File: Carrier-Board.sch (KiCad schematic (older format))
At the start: 39 parts, among them J1 CONN_3-6318491-6, J2 Conn_01x0, J3 Conn_02x26_Odd_Even, J4 SI-51009-F, J5 Conn_02x26_Odd_Even, J6 Conn_01x03_Male, J7 Conn_01x03_Male, J8 Conn_01x06_Male, J9 Conn_02x04_Odd_Even, U1 MPM3620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

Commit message: Notes
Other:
- note added: "Pixie Wranglers:\nPrabodh Jhaveri \nChandler Griscom\n"
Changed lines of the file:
@@
 Text Notes 11600 700  0    60   ~ 0
 PC104\n
+Text Notes 9450 10900 0    60   ~ 0
+Pixie Wranglers:\nPrabodh Jhaveri \nChandler Griscom\n
 $EndSCHEMATC

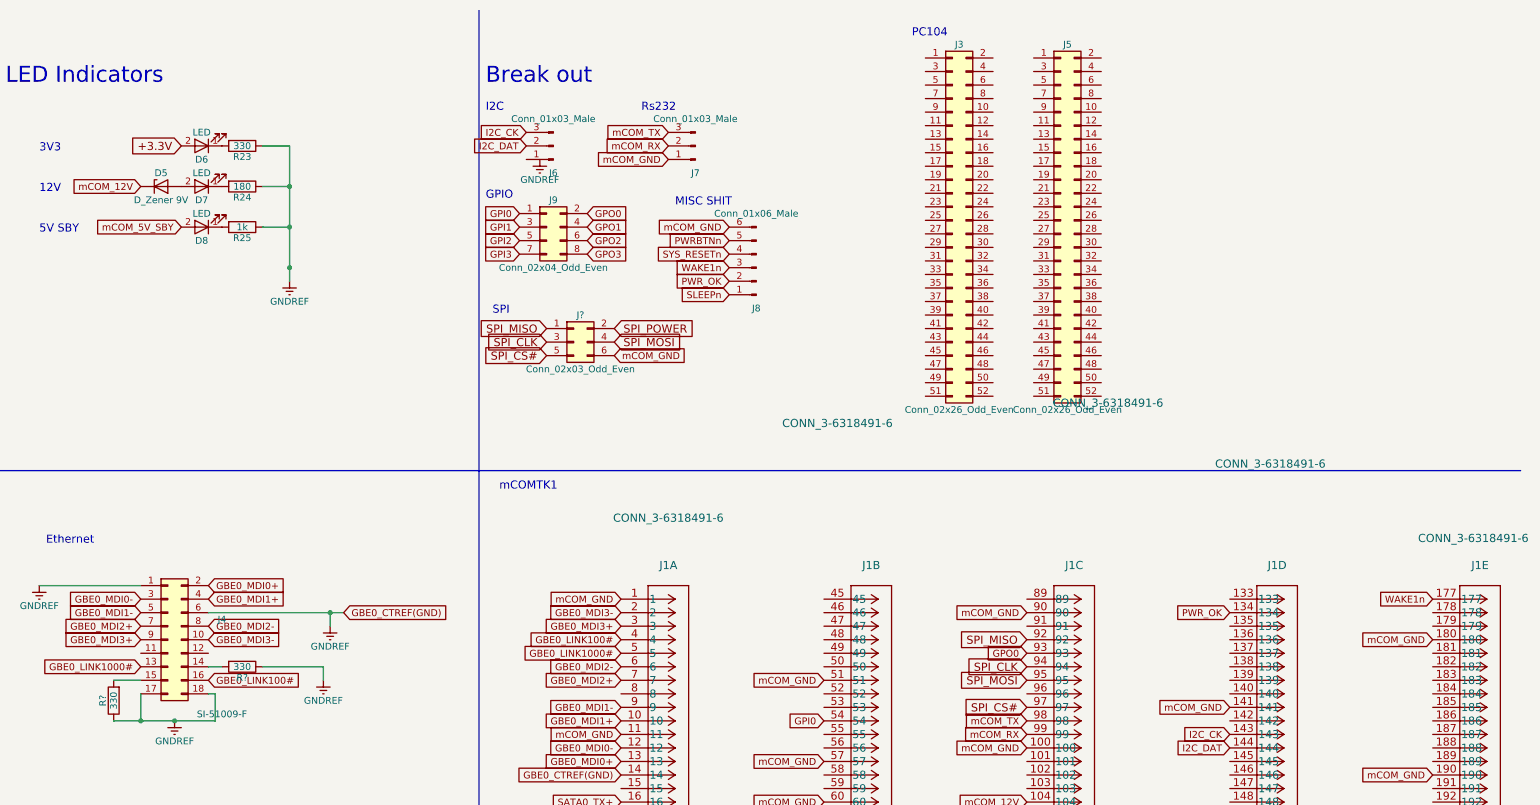
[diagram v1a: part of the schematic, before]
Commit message: added buttons
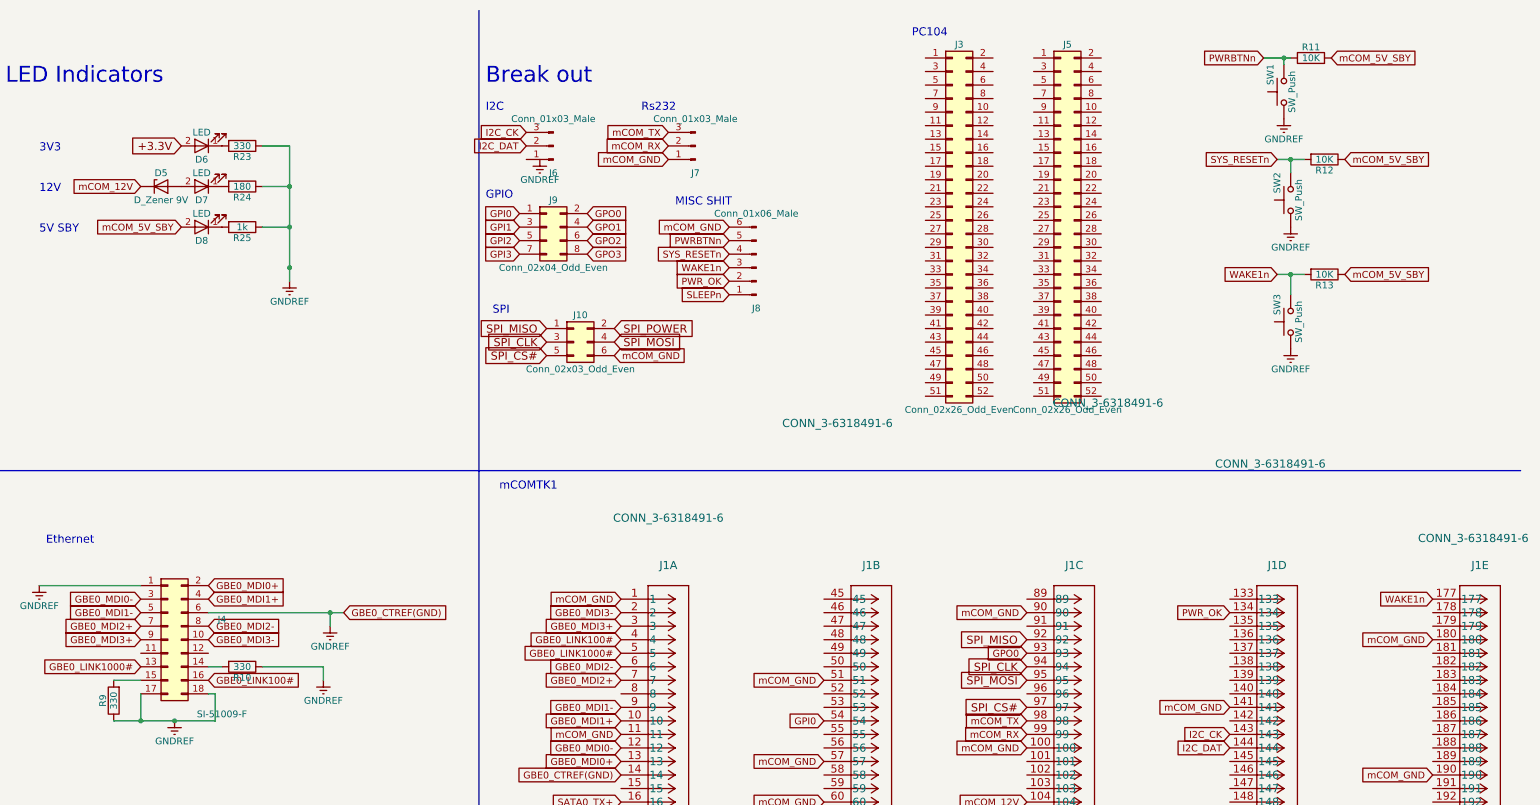
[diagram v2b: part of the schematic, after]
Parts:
- added R11, R12, R13: 10K, symbol R
- added SW1, SW2, SW3: SW_Push, Buttons_Switches_SMD:SW_SPST_PTS645, symbol SW_Push
- J10: renamed from J?; footprint (none) -> Pin_Headers:Pin_Header_Angled_2x03_Pitch2.54mm
- gave numbers to parts that had none: 2
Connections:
- net +5V: now also R11.2, R12.1, R13.1
- net GNDREF: now also SW1.1, SW2.1, SW3.1
- net PWRBTNn: now also R11.1, SW1.2
- net SYS_RESETn: now also R12.2, SW2.2
- net WAKE1n: now also R13.2, SW3.2

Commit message: Change but3ton footprint
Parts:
- SW1, SW2, SW3: footprint Buttons_Switches_SMD:SW_SPST_PTS645 -> Buttons_Switches_SMD:SW_SPST_B3U-1000P
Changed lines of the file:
@@
 LIBS:Carrier-Board
 LIBS:SI-51009-F
+LIBS:MCP6H04-E
+LIBS:BusSimulator
 LIBS:Carrier-Board-cache
 EELAYER 25 0
@@
 F 0 "SW2" H 14450 2000 50  0000 L CNN
 F 1 "SW_Push" H 14400 1840 50  0000 C CNN
-F 2 "Buttons_Switches_SMD:SW_SPST_PTS645" H 14400 2100 50  0001 C CNN
+F 2 "Buttons_Switches_SMD:SW_SPST_B3U-1000P" H 14400 2100 50  0001 C CNN
 F 3 "" H 14400 2100 50  0001 C CNN
 	1    14400 1900
@@
 F 0 "SW3" H 14450 2900 50  0000 L CNN
 F 1 "SW_Push" H 14400 2740 50  0000 C CNN
-F 2 "Buttons_Switches_SMD:SW_SPST_PTS645" H 14400 3000 50  0001 C CNN
+F 2 "Buttons_Switches_SMD:SW_SPST_B3U-1000P" H 14400 3000 50  0001 C CNN
 F 3 "" H 14400 3000 50  0001 C CNN
 	1    14400 2800
@@
 F 0 "SW1" H 14400 1200 50  0000 L CNN
 F 1 "SW_Push" H 14350 1040 50  0000 C CNN
-F 2 "Buttons_Switches_SMD:SW_SPST_PTS645" H 14350 1300 50  0001 C CNN
+F 2 "Buttons_Switches_SMD:SW_SPST_B3U-1000P" H 14350 1300 50  0001 C CNN
 F 3 "" H 14350 1300 50  0001 C CNN
 	1    14350 1100

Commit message: started traces
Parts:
- C1, C2, C3, C4: footprint BusSimulator:C22 -> Capacitors_SMD:C_0805
- R10: footprint (none) -> Resistors_SMD:R_0805
- R11, R12, R13: footprint (none) -> Resistors_SMD:R_0603
- renumbered D7 to D6, D6 to D7
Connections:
- net GNDREF: now also J6.1 (Pin_1)
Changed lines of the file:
@@
 LIBS:Carrier-Board
 LIBS:SI-51009-F
-LIBS:MCP6H04-E
-LIBS:BusSimulator
 LIBS:Carrier-Board-cache
 EELAYER 25 0
@@
 F 0 "C2" V 3075 3625 60  0000 C CNN
 F 1 "22uF" V 3000 3575 60  0000 C CNN
-F 2 "BusSimulator:C22" H 3150 3040 60  0001 C CNN
+F 2 "Capacitors_SMD:C_0805" H 3150 3040 60  0001 C CNN
 F 3 "" H 3000 3400 60  0000 C CNN
 	1    3000 3400
@@
 F 0 "C1" V 2525 1425 60  0000 C CNN
 F 1 "10uF" V 2425 1375 60  0000 C CNN
-F 2 "BusSimulator:C22" H 2650 990 60  0001 C CNN
+F 2 "Capacitors_SMD:C_0805" H 2650 990 60  0001 C CNN
 F 3 "" H 2500 1350 60  0000 C CNN
 	1    2500 1350
@@
 F 0 "C4" V 3025 6625 60  0000 C CNN
 F 1 "22uF" V 2950 6575 60  0000 C CNN
-F 2 "BusSimulator:C22" H 3100 6040 60  0001 C CNN
+F 2 "Capacitors_SMD:C_0805" H 3100 6040 60  0001 C CNN
 F 3 "" H 2950 6400 60  0000 C CNN
 	1    2950 6400
@@
 F 0 "C3" V 2475 4425 60  0000 C CNN
 F 1 "10uF" V 2375 4375 60  0000 C CNN
-F 2 "BusSimulator:C22" H 2600 3990 60  0001 C CNN
+F 2 "Capacitors_SMD:C_0805" H 2600 3990 60  0001 C CNN
 F 3 "" H 2450 4350 60  0000 C CNN
 	1    2450 4350
@@
 Break out\n
 $Comp
-L LED D6
+L LED D7
 U 1 1 5A07DE5B
 P 6350 1500
-F 0 "D6" H 6350 1600 50  0000 C CNN
+F 0 "D7" H 6350 1600 50  0000 C CNN
 F 1 "LED" H 6350 1400 50  0000 C CNN
 F 2 "Diodes_SMD:D_1206" H 6350 1500 50  0001 C CNN
@@
 LED Indicators\n
 $Comp
-L LED D7
+L LED D6
 U 1 1 5A08439E
 P 6350 1800
-F 0 "D7" H 6350 1900 50  0000 C CNN
+F 0 "D6" H 6350 1900 50  0000 C CNN
 F 1 "LED" H 6350 1700 50  0000 C CNN
 F 2 "Diodes_SMD:D_1206" H 6350 1800 50  0001 C CNN
@@
 L GNDREF #PWR036
 U 1 1 5A0B68CF
-P 8850 1600
-F 0 "#PWR036" H 8850 1350 50  0001 C CNN
-F 1 "GNDREF" H 8850 1450 50  0000 C CNN
-F 2 "" H 8850 1600 50  0001 C CNN
-F 3 "" H 8850 1600 50  0001 C CNN
-	1    8850 1600
+P 8750 1600
+F 0 "#PWR036" H 8750 1350 50  0001 C CNN
+F 1 "GNDREF" H 8750 1450 50  0000 C CNN
+F 2 "" H 8750 1600 50  0001 C CNN
+F 3 "" H 8750 1600 50  0001 C CNN
+	1    8750 1600
 	1    0    0    -1
 $EndComp
@@
 F 0 "R10" V 6730 5350 50  0000 C CNN
 F 1 "330" V 6650 5350 50  0000 C CNN
-F 2 "" V 6580 5350 50  0001 C CNN
+F 2 "Resistors_SMD:R_0805" V 6580 5350 50  0001 C CNN
 F 3 "" H 6650 5350 50  0001 C CNN
 	1    6650 5350
@@
 F 0 "R11" V 14630 850 50  0000 C CNN
 F 1 "10K" V 14550 850 50  0000 C CNN
-F 2 "" V 14480 850 50  0001 C CNN
+F 2 "Resistors_SMD:R_0603" V 14480 850 50  0001 C CNN
 F 3 "" H 14550 850 50  0001 C CNN
 	1    14550 850
@@
 F 0 "R12" V 14730 1600 50  0000 C CNN
 F 1 "10K" V 14650 1600 50  0000 C CNN
-F 2 "" V 14580 1600 50  0001 C CNN
+F 2 "Resistors_SMD:R_0603" V 14580 1600 50  0001 C CNN
 F 3 "" H 14650 1600 50  0001 C CNN
 	1    14650 1600
@@
 F 0 "R13" V 14730 2450 50  0000 C CNN
 F 1 "10K" V 14650 2450 50  0000 C CNN
-F 2 "" V 14580 2450 50  0001 C CNN
+F 2 "Resistors_SMD:R_0603" V 14580 2450 50  0001 C CNN
 F 3 "" H 14650 2450 50  0001 C CNN
 	1    14650 2450

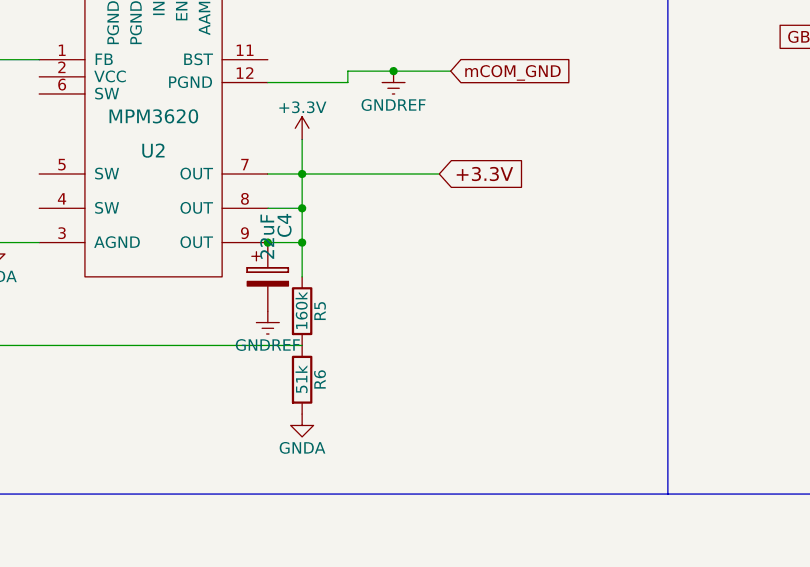
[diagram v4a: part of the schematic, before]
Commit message: Finished Traces
No camera
needs verification
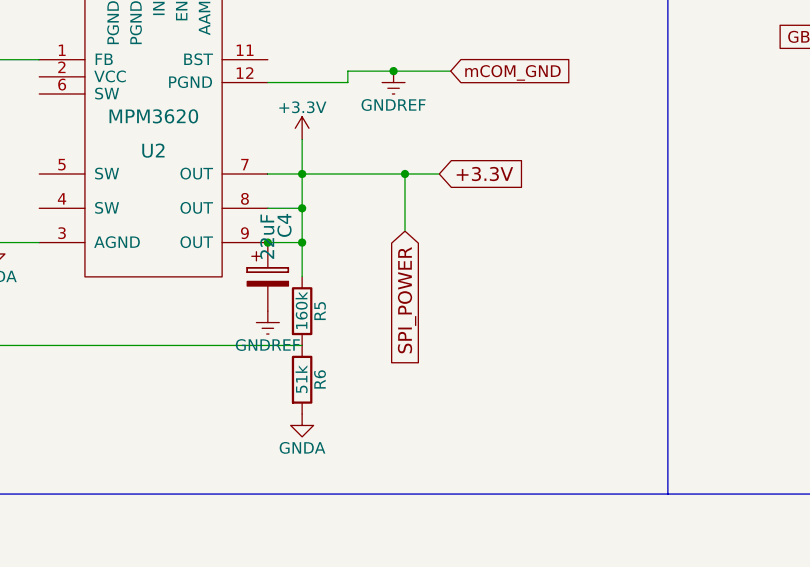
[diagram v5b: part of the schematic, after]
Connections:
- net SPI_POWER is gone; now on net +3V3: J10.2 (Pin_2)
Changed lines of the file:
@@
 Text GLabel 14800 2450 2    51   Input ~ 0
 mCOM_5V_SBY
+Text GLabel 3550 6200 3    60   Input ~ 0
+SPI_POWER
+Connection ~ 3550 5950
+Wire Wire Line
+	3550 5950 3550 6200
 $EndSCHEMATC
